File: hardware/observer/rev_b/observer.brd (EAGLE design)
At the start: 47.8 x 59.9 mm, 38 parts, among them J1 CON_HEADER_2X05-SMD+SHROUDED, J2 CON_HEADER_2X05-SMD+SHROUDED, J3 TC2030-CC2538-BL-NL, J4 JUMPER-PTH-2-NO, J5 PINHD-2X8/SMD, J6 CON_HEADER_2X05-PTH+SHROUDED_A, P9/P8 BBB_HEADER, U1 LPS331AP, U2 MPU-9250, U3 SI1147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

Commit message: started routing
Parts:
- moved H6 45.8 mm to (43.4, 14.0), turned to 180 degrees
- moved H7 45.8 mm to (11.2, 14.0), turned to 180 degrees
- moved H5 45.4 mm to (43.4, 46.2), turned to 180 degrees
- moved H8 45.4 mm to (11.2, 46.2)
- moved LOGO1 42.4 mm to (8.81, 19.8)
- moved D1 40.3 mm to (36.3, 12.2), turned to 0 degrees
- moved D3 40.3 mm to (18.3, 12.2), turned to 0 degrees
- moved J3 37.9 mm to (17.5, 46.5), turned to 90 degrees
- moved U4 36.8 mm to (27.3, 11.8), turned to 180 degrees
- moved C10 35.4 mm to (38.5, 16.5), turned to 0 degrees
- moved U6 32.6 mm to (42.2, 37.0), turned to 135 degrees
- moved J5 30.7 mm to (29.0, 45.5), turned to 180 degrees
- moved J1 29.9 mm to (12.4, 31.8), turned to 90 degrees
- moved J2 29.9 mm to (12.4, 31.8), turned to 90 degrees
- moved R2 29.1 mm to (26.4, 77.5)
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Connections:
- new net EEPROM_SCL: P9/P8.P9_19, U7.SCL
- new net EEPROM_SDA: P9/P8.P9_20, U7.SDA
- net SCL: no longer P9/P8.P9_19, U7.SCL
- net SDA: no longer P9/P8.P9_20, U7.SDA
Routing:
- net 5V: track 6.22 -> 85.2 mm, vias 1 -> 2
- net BBB_MISO: track 16.9 -> 60.1 mm, vias 1 -> 4
- net BBB_SCLK: track 15.0 -> 56.5 mm, vias 1 -> 3
- net BBB_MOSI: track 18.2 -> 59.2 mm, vias 1 -> 3
- net OBSERVER_INT: track 0.00 -> 31.7 mm
- net !OBSERVER_CS: track 38.0 -> 13.4 mm, vias 2 -> 1
- net VCC: track 171.5 -> 155.0 mm
- net N$31: track 12.0 -> 0.00 mm
- net EEPROM_SDA: track 0.00 -> 6.02 mm, vias 0 -> 1
- net VDD: track 0.00 -> 2.54 mm
- net GND: vias 23 -> 22
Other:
- outline, holes or cut-outs redrawn

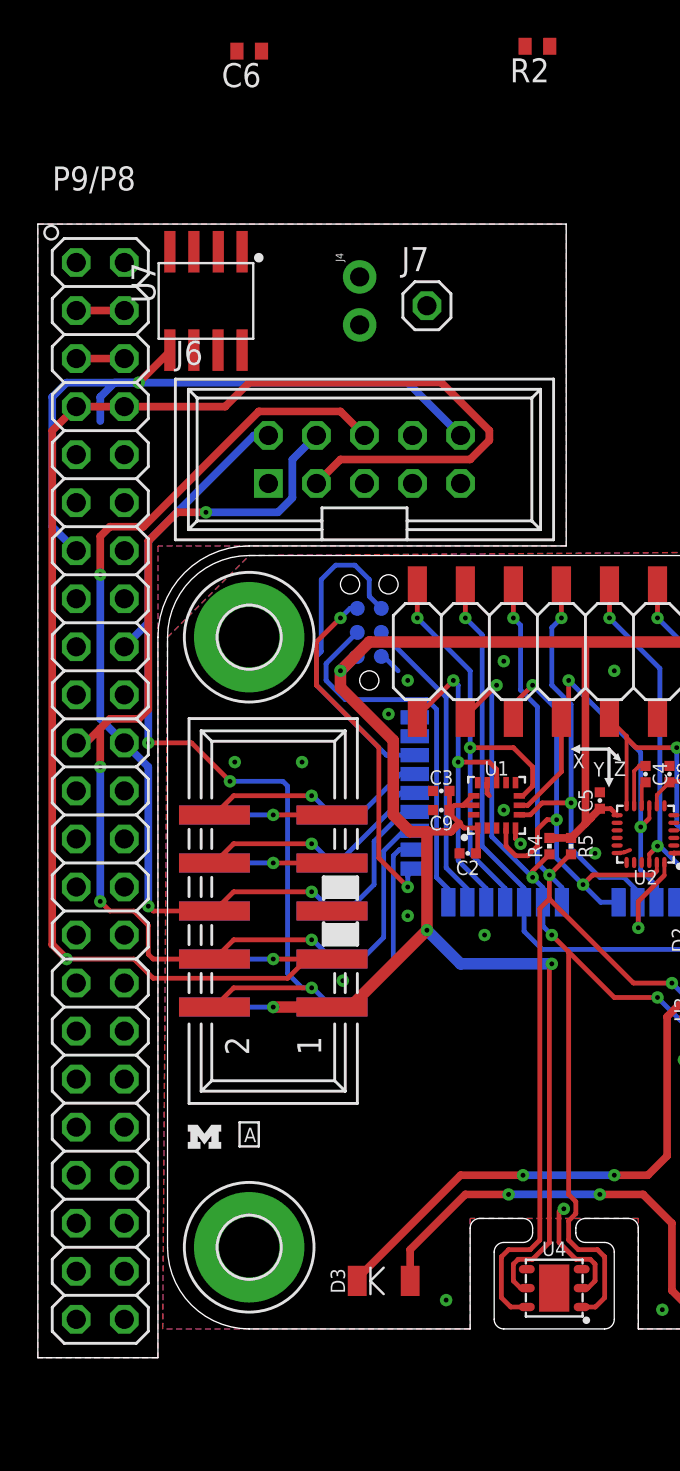
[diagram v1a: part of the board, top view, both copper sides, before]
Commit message: Finished routing header signals, need to add mousebites and microphone hardware
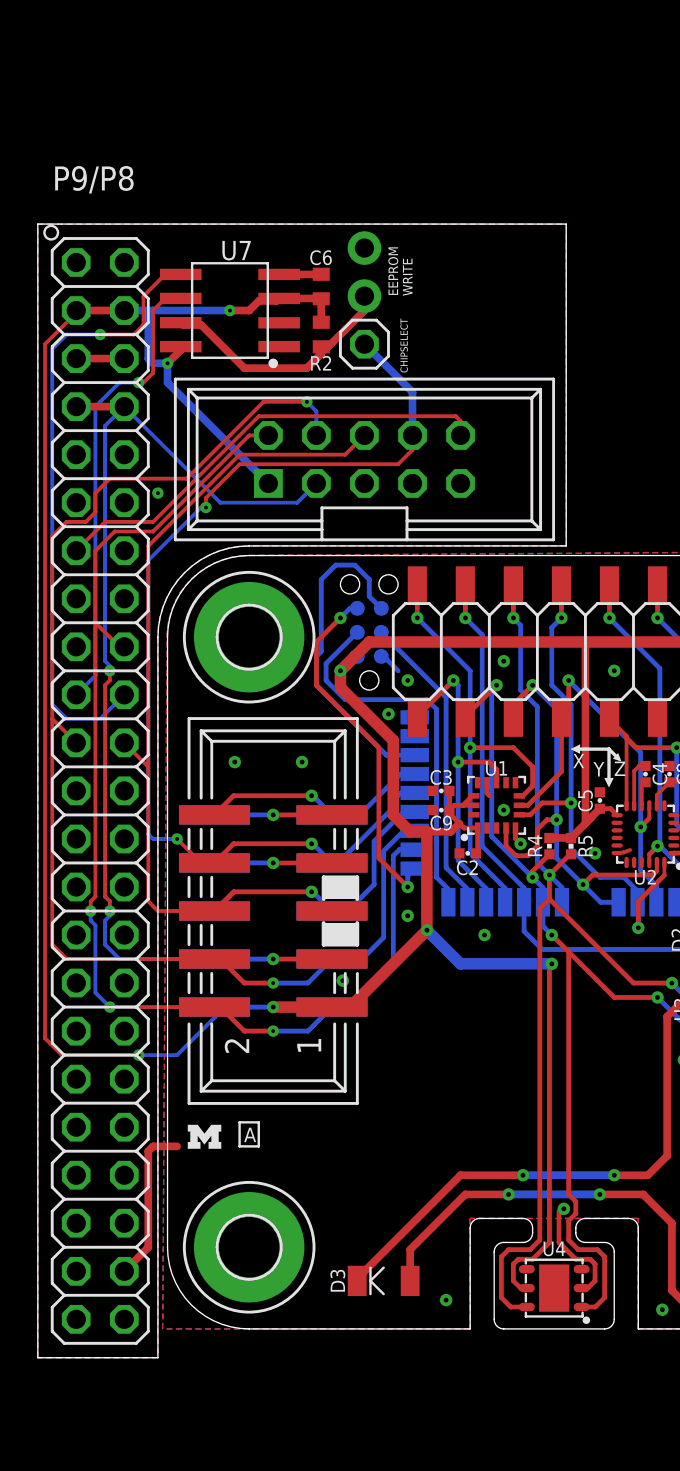
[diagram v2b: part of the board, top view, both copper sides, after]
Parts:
- moved R2 19.1 mm to (15.0, 62.2), turned to 270 degrees
- moved C6 13.0 mm to (15.0, 64.8), turned to 90 degrees
- moved J7 3.88 mm to (17.3, 61.7)
- moved J4 1.55 mm to (17.3, 65.5), turned to 90 degrees
- moved U7 1.37 mm to (10.2, 63.5), turned to 180 degrees
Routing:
- net VCC: track 155.0 -> 230.3 mm, vias 8 -> 11
- net !OBSERVER_CS: track 13.4 -> 55.3 mm, vias 1 -> 3
- net 5V: track 85.2 -> 56.8 mm, vias 2 -> 3
- net EEPROM_SDA: track 6.02 -> 32.9 mm
- net EEPROM_SCL: track 0.00 -> 24.8 mm, vias 0 -> 1
- net N$31: track 0.00 -> 12.9 mm
- net GND: track 19.0 -> 29.8 mm
- net BBB_MISO: track 60.1 -> 68.4 mm, vias 4 -> 2
- net OBSERVER_INT: track 31.7 -> 24.1 mm
- net BBB_MOSI: track 59.2 -> 62.3 mm
- net BBB_SCLK: track 56.5 -> 54.6 mm, vias 3 -> 1
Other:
- board text added: "CHIPSELECT"
- board text added: "EEPROM WRITE"

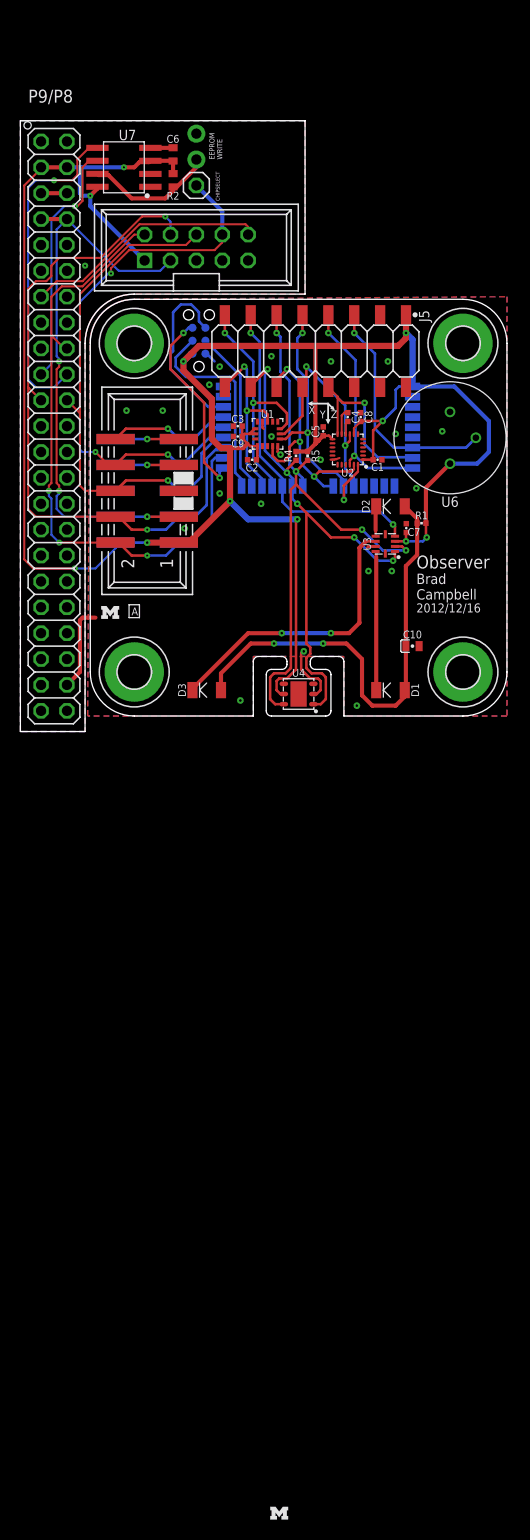
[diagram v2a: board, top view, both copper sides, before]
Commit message: added mic and opamp to sch
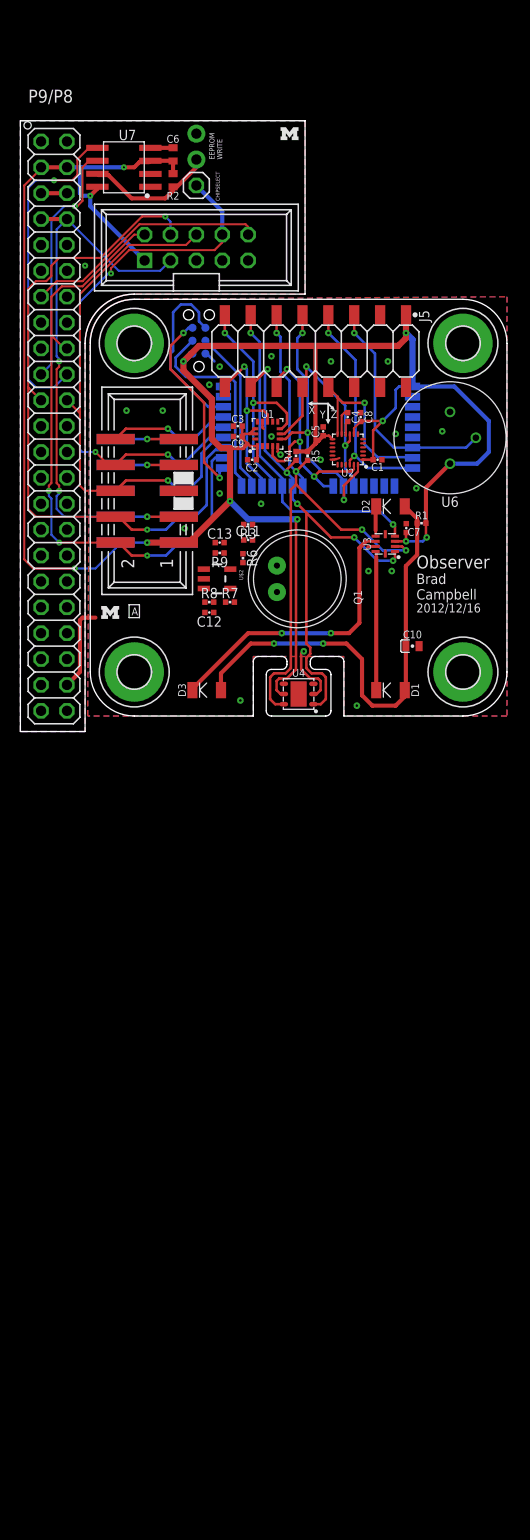
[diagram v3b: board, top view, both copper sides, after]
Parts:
- added C11, C12: 4.7uF, passives:0402_CAP
- added C13: 12pF, passives:0402_CAP
- added Q1: (no value), observer:ELECTRET_9.7
- added R3: 2.2k, passives:0402_RES
- added R6, R7, R8: 10k, passives:0402_RES
- added R9: 1M, passives:0402_RES
- added U$2: OPA344, SparkFun-AnalogIC:SOT23-5
- moved LOGO2 135.4 mm to (26.4, 66.8)
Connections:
- net UN renamed MIC_INT
- new net MIC_AIN: C13.1, R9.2, U$2.1
- new net N$1: C11.2, Q1.+, R3.1
- new net N$10: C12.1, R7.1, R8.2, U$2.3
- new net N$5: C11.1, R6.1
- new net N$9: R6.2, R9.1, U$2.4
- net GND: now also C12.2, Q1.-, R8.1, U$2.2
- net VCC: now also R3.2, R7.2, U$2.5
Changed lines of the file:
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@@
 <attribute name="VALUE" x="28.956" y="51.308" size="1.016" layer="27" font="vector" ratio="12" rot="R180" align="bottom-center"/>
 </element>
-<element name="LOGO2" library="logos" package="UMICH_SOLID_50MIL" value="UMICH_SOLID_TINY" x="25.4" y="-68.58"/>
+<element name="LOGO2" library="logos" package="UMICH_SOLID_50MIL" value="UMICH_SOLID_TINY" x="26.416" y="66.802"/>
 <element name="P9/P8" library="observer" package="BBB_HEADERS" value="BBB_HEADER" x="0.762" y="8.89"/>
 <element name="U7" library="bbb-cc2520" package="CAT24C256WI-GT3" value="CAT24C256WI-GT3" x="10.16" y="63.5" smashed="yes" rot="R180">
@@
 <attribute name="VALUE" x="16.002" y="58.547" size="1.27" layer="27"/>
 </element>
+<element name="Q1" library="observer" package="ELECTRET_9.7" value="" x="27.178" y="23.114" rot="R90"/>
+<element name="U$2" library="SparkFun-AnalogIC" package="SOT23-5" value="OPA344" x="19.304" y="23.114" rot="R270"/>
+<element name="R3" library="passives" package="0402_RES" value="2.2k" x="22.352" y="28.448" rot="R180"/>
+<element name="C11" library="passives" package="0402_CAP" value="4.7uF" x="22.352" y="26.924"/>
+<element name="R6" library="passives" package="0402_RES" value="10k" x="21.844" y="25.146" rot="R270"/>
+<element name="R7" library="passives" package="0402_RES" value="10k" x="20.574" y="20.828"/>
+<element name="R8" library="passives" package="0402_RES" value="10k" x="18.542" y="20.828"/>
+<element name="C12" library="passives" package="0402_CAP" value="4.7uF" x="18.542" y="19.812" rot="R180"/>
+<element name="R9" library="passives" package="0402_RES" value="1M" x="19.558" y="25.654" rot="R180"/>
+<element name="C13" library="passives" package="0402_CAP" value="12pF" x="19.558" y="26.67"/>
 </elements>
 <signals>
@@
 <wire x1="6.858" y1="60.706" x2="6.858" y2="59.69" width="0.4064" layer="16"/>
 <wire x1="6.858" y1="59.69" x2="12.192" y2="54.356" width="0.4064" layer="16"/>
+<contactref element="R3" pad="2"/>
+<contactref element="U$2" pad="5"/>
+<contactref element="R7" pad="2"/>
+<wire x1="21.91893125" y1="28.448" x2="20.6041" y2="24.064" width="0" layer="19" extent="1-1"/>
+<wire x1="21.00706875" y1="20.828" x2="21.91893125" y2="28.448" width="0" layer="19" extent="1-1"/>
+<wire x1="16.51" y1="26.67" x2="21.91893125" y2="28.448" width="0" layer="19" extent="1-1"/>
 </signal>
 <signal name="GND">
@@
 <wire x1="12.76" y1="65.41" x2="14.976" y2="65.41" width="0.4064" layer="1"/>
 <wire x1="14.976" y1="65.41" x2="14.986" y2="65.42" width="0.4064" layer="1"/>
+<contactref element="Q1" pad="-"/>
+<contactref element="C12" pad="2"/>
+<contactref element="R8" pad="1"/>
+<contactref element="U$2" pad="2"/>
 </signal>
 <signal name="N$3">
@@
 <wire x1="32.766" y1="47.244" x2="32.766" y2="49.022" width="0.254" layer="1"/>
 </signal>
-<signal name="UN">
+<signal name="MIC_INT">
 <contactref element="U5" pad="6"/>
 </signal>
@@
 <via x="6.35" y="53.848" extent="1-16" drill="0.2032"/>
 </signal>
+<signal name="N$1">
+<contactref element="Q1" pad="+"/>
+<contactref element="R3" pad="1"/>
+<contactref element="C11" pad="2"/>
+<wire x1="22.78506875" y1="26.924" x2="25.178" y2="24.414" width="0" layer="19" extent="1-1"/>
+<wire x1="22.78506875" y1="28.448" x2="22.78506875" y2="26.924" width="0" layer="19" extent="1-1"/>
+</signal>
+<signal name="N$5">
+<contactref element="C11" pad="1"/>
+<contactref element="R6" pad="1"/>
+<wire x1="21.844" y1="25.57906875" x2="21.91893125" y2="26.924" width="0" layer="19" extent="1-1"/>
+</signal>
+<signal name="N$9">
+<contactref element="R6" pad="2"/>
+<contactref element="U$2" pad="4"/>
+<contactref element="R9" pad="1"/>
+<wire x1="21.844" y1="24.71293125" x2="20.6041" y2="22.164" width="0" layer="19" extent="1-1"/>
+<wire x1="19.99106875" y1="25.654" x2="21.844" y2="24.71293125" width="0" layer="19" extent="1-1"/>
+</signal>
+<signal name="N$10">
+<contactref element="R8" pad="2"/>
+<contactref element="R7" pad="1"/>
+<contactref element="C12" pad="1"/>
+<contactref element="U$2" pad="3"/>
+<wire x1="18.0039" y1="22.164" x2="20.14093125" y2="20.828" width="0" layer="19" extent="1-1"/>
+<wire x1="18.97506875" y1="20.828" x2="20.14093125" y2="20.828" width="0" layer="19" extent="1-1"/>
+<wire x1="18.97506875" y1="19.812" x2="18.97506875" y2="20.828" width="0" layer="19" extent="1-1"/>
+</signal>
+<signal name="MIC_AIN">
+<contactref element="C13" pad="1"/>
+<contactref element="U$2" pad="1"/>
+<contactref element="R9" pad="2"/>
+<wire x1="19.12493125" y1="25.654" x2="18.0039" y2="24.064" width="0" layer="19" extent="1-1"/>
+<wire x1="19.12493125" y1="26.67" x2="19.12493125" y2="25.654" width="0" layer="19" extent="1-1"/>
+</signal>
 </signals>

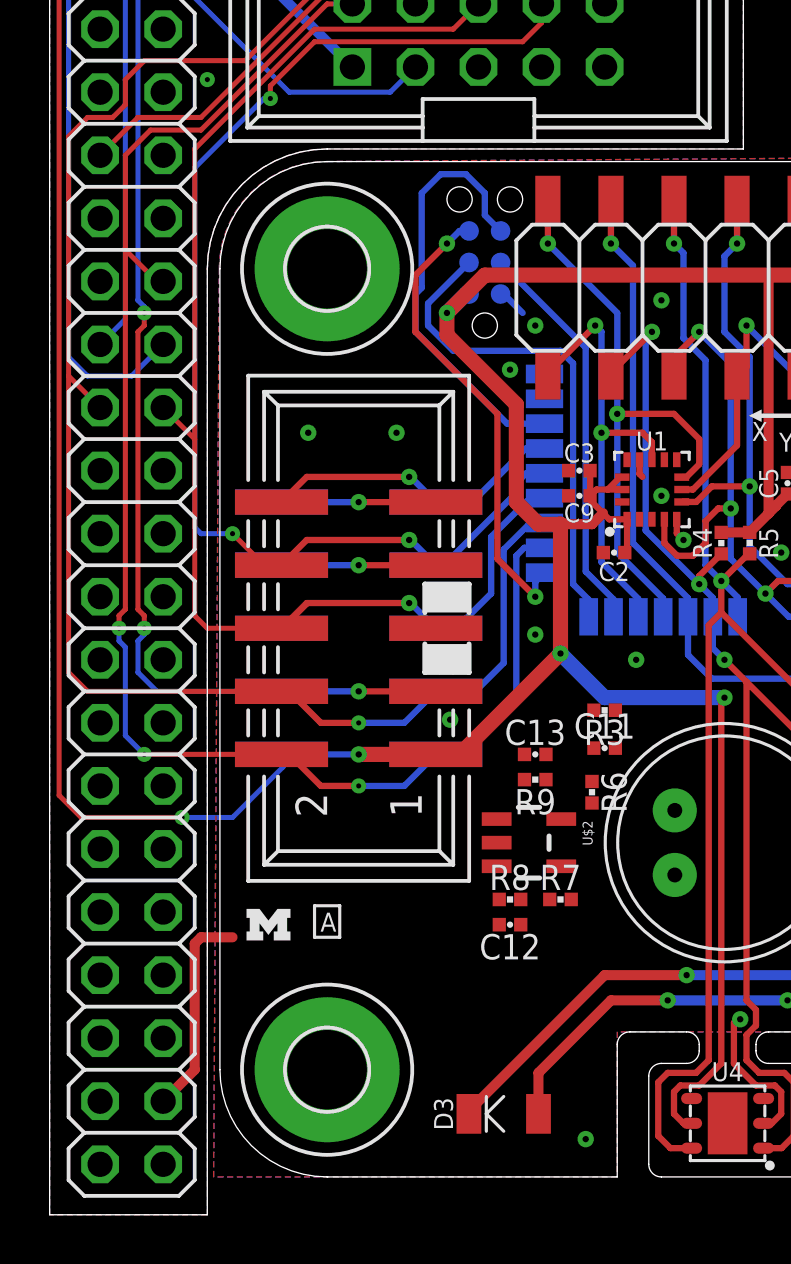
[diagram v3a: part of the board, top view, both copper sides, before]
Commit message: added mousebites
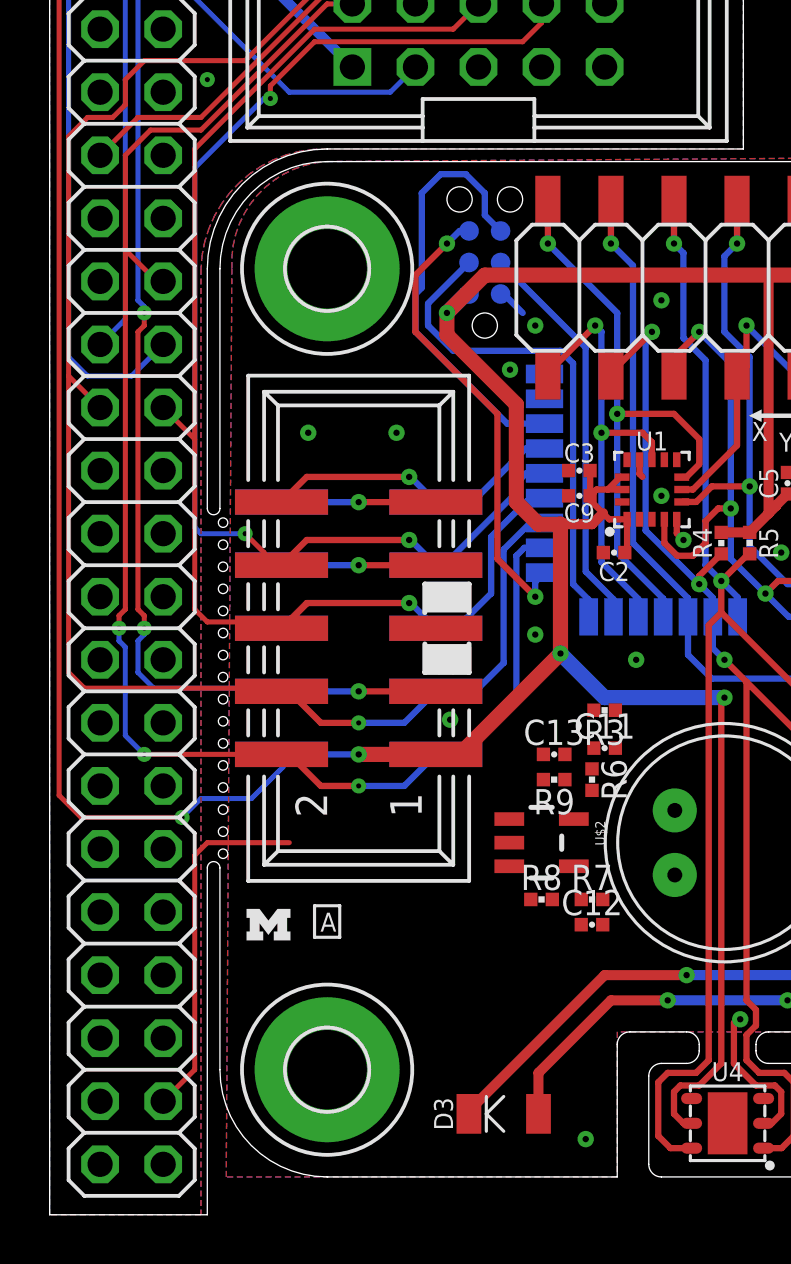
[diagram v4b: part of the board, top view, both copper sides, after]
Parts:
- moved C12 3.30 mm to (21.8, 19.8), turned to 0 degrees
- moved R7 1.27 mm to (21.8, 20.8)
- moved R8 1.27 mm to (19.8, 20.8)
- moved C13 0.76 mm to (20.3, 26.7)
- moved R9 0.76 mm to (20.3, 25.7)
- moved U$2 0.51 mm to (19.8, 23.1)
- moved R6 0.51 mm to (21.8, 25.7)
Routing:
- net GND: track 29.8 -> 35.7 mm
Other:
- outline, holes or cut-outs redrawn
